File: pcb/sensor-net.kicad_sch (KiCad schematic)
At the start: 14 parts, among them U4 M24C32-FMN, U5 MS5607-02BA, U6 LIS2MDL, U7 LSM6DSO32TR, U8 SAM-M8Q

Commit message: Filled out the BOM for the schematic. Consolidated some components and changed footprint sizes.
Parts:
- C16, C17, C19, C20, C23, C24: footprint Capacitor_SMD:C_0201_0603Metric -> Capacitor_SMD:C_0402_1005Metric; MP (none) -> GRM155R61A104KA01J
- C18: footprint Capacitor_SMD:C_0805_2012Metric -> Capacitor_SMD:C_0603_1608Metric; MP (none) -> C1608X5R0J106K080AB
- C21: MP (none) -> 0603B204K160CT
- C22: MP (none) -> CGA3E1X5R0J475K080AC
- U4: MP (none) -> M24C32-FMN6TP
- U5: MP (none) -> MS560702BA03-50
- U6: MP (none) -> LIS2MDLTR
- U7: MP (none) -> LSM6DSO32TR
- U8: MP (none) -> SAM-M8Q-0
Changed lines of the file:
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@@
 			)
 		)
-		(property "Datasheet" "~"
+		(property "Datasheet" "https://www.mouser.ca/datasheet/2/210/WTC_MLCC_General_Purpose-1534899.pdf"
 			(at 152.4 59.69 0)
 			(effects
@@
 			)
 		)
+		(property "MP" "0603B204K160CT"
+			(at 152.4 59.69 0)
+			(effects
+				(font
+					(size 1.27 1.27)
+				)
+				(hide yes)
+			)
+		)
 		(pin "2"
 		)
@@
 			)
 		)
-		(property "Footprint" "Capacitor_SMD:C_0201_0603Metric"
+		(property "Footprint" "Capacitor_SMD:C_0402_1005Metric"
 			(at 249.8852 107.95 0)
 			(effects
@@
 			)
 		)
-		(property "Datasheet" "~"
+		(property "Datasheet" "https://www.mouser.ca/datasheet/2/281/1/GRM155R61A104KA01_02A-1983866.pdf"
 			(at 248.92 104.14 0)
 			(effects
@@
 			)
 		)
+		(property "MP" "GRM155R61A104KA01J "
+			(at 248.92 104.14 0)
+			(effects
+				(font
+					(size 1.27 1.27)
+				)
+				(hide yes)
+			)
+		)
 		(pin "1"
 		)
@@
 			)
 		)
-		(property "Footprint" "Capacitor_SMD:C_0805_2012Metric"
+		(property "Footprint" "Capacitor_SMD:C_0603_1608Metric"
 			(at 176.2252 43.18 0)
 			(effects
@@
 			)
 		)
-		(property "Datasheet" "~"
+		(property "Datasheet" "https://product.tdk.com/system/files/dam/doc/product/capacitor/ceramic/mlcc/catalog/mlcc_commercial_general_en.pdf?ref_disty=mouser"
 			(at 175.26 39.37 0)
 			(effects
@@
 			)
 		)
+		(property "MP" "C1608X5R0J106K080AB"
+			(at 175.26 39.37 0)
+			(effects
+				(font
+					(size 1.27 1.27)
+				)
+				(hide yes)
+			)
+		)
 		(pin "2"
 		)
@@
 			)
 		)
+		(property "MP" "M24C32-FMN6TP"
+			(at 226.06 48.26 0)
+			(effects
+				(font
+					(size 1.27 1.27)
+				)
+				(hide yes)
+			)
+		)
 		(pin "8"
 		)
@@
 			)
 		)
+		(property "MP" "LIS2MDLTR"
+			(at 137.16 50.8 0)
+			(effects
+				(font
+					(size 1.27 1.27)
+				)
+				(hide yes)
+			)
+		)
 		(pin "9"
 		)
@@
 			)
 		)
-		(property "Footprint" "Capacitor_SMD:C_0201_0603Metric"
+		(property "Footprint" "Capacitor_SMD:C_0402_1005Metric"
 			(at 164.7952 43.18 0)
 			(effects
@@
 			)
 		)
-		(property "Datasheet" "~"
+		(property "Datasheet" "https://www.mouser.ca/datasheet/2/281/1/GRM155R61A104KA01_02A-1983866.pdf"
 			(at 163.83 39.37 0)
 			(effects
@@
 			)
 		)
+		(property "MP" "GRM155R61A104KA01J "
+			(at 163.83 39.37 0)
+			(effects
+				(font
+					(size 1.27 1.27)
+				)
+				(hide yes)
+			)
+		)
 		(pin "2"
 		)
@@
 			)
 		)
-		(property "Footprint" "Capacitor_SMD:C_0201_0603Metric"
+		(property "Footprint" "Capacitor_SMD:C_0402_1005Metric"
 			(at 238.4552 107.95 0)
 			(effects
@@
 			)
 		)
-		(property "Datasheet" "~"
+		(property "Datasheet" "https://www.mouser.ca/datasheet/2/281/1/GRM155R61A104KA01_02A-1983866.pdf"
 			(at 237.49 104.14 0)
 			(effects
@@
 			)
 		)
+		(property "MP" "GRM155R61A104KA01J "
+			(at 237.49 104.14 0)
+			(effects
+				(font
+					(size 1.27 1.27)
+				)
+				(hide yes)
+			)
+		)
 		(pin "1"
 		)
@@
 			)
 		)
-		(property "Footprint" "Capacitor_SMD:C_0201_0603Metric"
+		(property "Footprint" "Capacitor_SMD:C_0402_1005Metric"
 			(at 152.0952 43.18 0)
 			(effects
@@
 			)
 		)
-		(property "Datasheet" "~"
+		(property "Datasheet" "https://www.mouser.ca/datasheet/2/281/1/GRM155R61A104KA01_02A-1983866.pdf"
 			(at 151.13 39.37 0)
 			(effects
@@
 			)
 		)
+		(property "MP" "GRM155R61A104KA01J "
+			(at 151.13 39.37 0)
+			(effects
+				(font
+					(size 1.27 1.27)
+				)
+				(hide yes)
+			)
+		)
 		(pin "2"
 		)
@@
 			)
 		)
-		(property "Footprint" "Capacitor_SMD:C_0201_0603Metric"
+		(property "Footprint" "Capacitor_SMD:C_0402_1005Metric"
 			(at 82.2452 54.61 0)
 			(effects
@@
 			)
 		)
-		(property "Datasheet" "~"
+		(property "Datasheet" "https://www.mouser.ca/datasheet/2/281/1/GRM155R61A104KA01_02A-1983866.pdf"
 			(at 81.28 50.8 0)
 			(effects
@@
 			)
 		)
+		(property "MP" "GRM155R61A104KA01J "
+			(at 81.28 50.8 0)
+			(effects
+				(font
+					(size 1.27 1.27)
+				)
+				(hide yes)
+			)
+		)
 		(pin "2"
 		)
@@
 			)
 		)
-		(property "Datasheet" "~"
+		(property "Datasheet" "https://product.tdk.com/system/files/dam/doc/product/capacitor/ceramic/mlcc/catalog/mlcc_automotive_general_en.pdf?ref_disty=mouser"
 			(at 88.9 96.52 0)
 			(effects
@@
 			)
 		)
+		(property "MP" "CGA3E1X5R0J475K080AC"
+			(at 88.9 96.52 0)
+			(effects
+				(font
+					(size 1.27 1.27)
+				)
+				(hide yes)
+			)
+		)
 		(pin "2"
 		)
@@
 			)
 		)
+		(property "MP" "MS560702BA03-50"
+			(at 63.5 49.53 0)
+			(effects
+				(font
+					(size 1.27 1.27)
+				)
+				(hide yes)
+			)
+		)
 		(pin "8"
 		)
@@
 			)
 		)
-		(property "Footprint" "Capacitor_SMD:C_0201_0603Metric"
+		(property "Footprint" "Capacitor_SMD:C_0402_1005Metric"
 			(at 211.7852 46.99 0)
 			(effects
@@
 			)
 		)
-		(property "Datasheet" "~"
+		(property "Datasheet" "https://www.mouser.ca/datasheet/2/281/1/GRM155R61A104KA01_02A-1983866.pdf"
 			(at 210.82 43.18 0)
 			(effects
@@
 			)
 		)
+		(property "MP" "GRM155R61A104KA01J "
+			(at 210.82 43.18 0)
+			(effects
+				(font
+					(size 1.27 1.27)
+				)
+				(hide yes)
+			)
+		)
 		(pin "1"
 		)
@@
 			)
 		)
+		(property "MP" "SAM-M8Q-0"
+			(at 71.12 114.3 0)
+			(effects
+				(font
+					(size 1.27 1.27)
+				)
+				(hide yes)
+			)
+		)
 		(pin "11"
 		)
@@
 			)
 		)
-		(property "Datasheet" ""
+		(property "Datasheet" "https://www.mouser.ca/datasheet/2/389/lsm6dso32-1815462.pdf"
 			(at 212.09 113.03 0)
 			(effects
@@
 				(hide yes)
 			)
+		)
+		(property "MP" "LSM6DSO32TR"
+			(at 212.09 113.03 0)
+			(effects
+				(font
+					(size 1.27 1.27)
+				)
+				(hide yes)
+			)

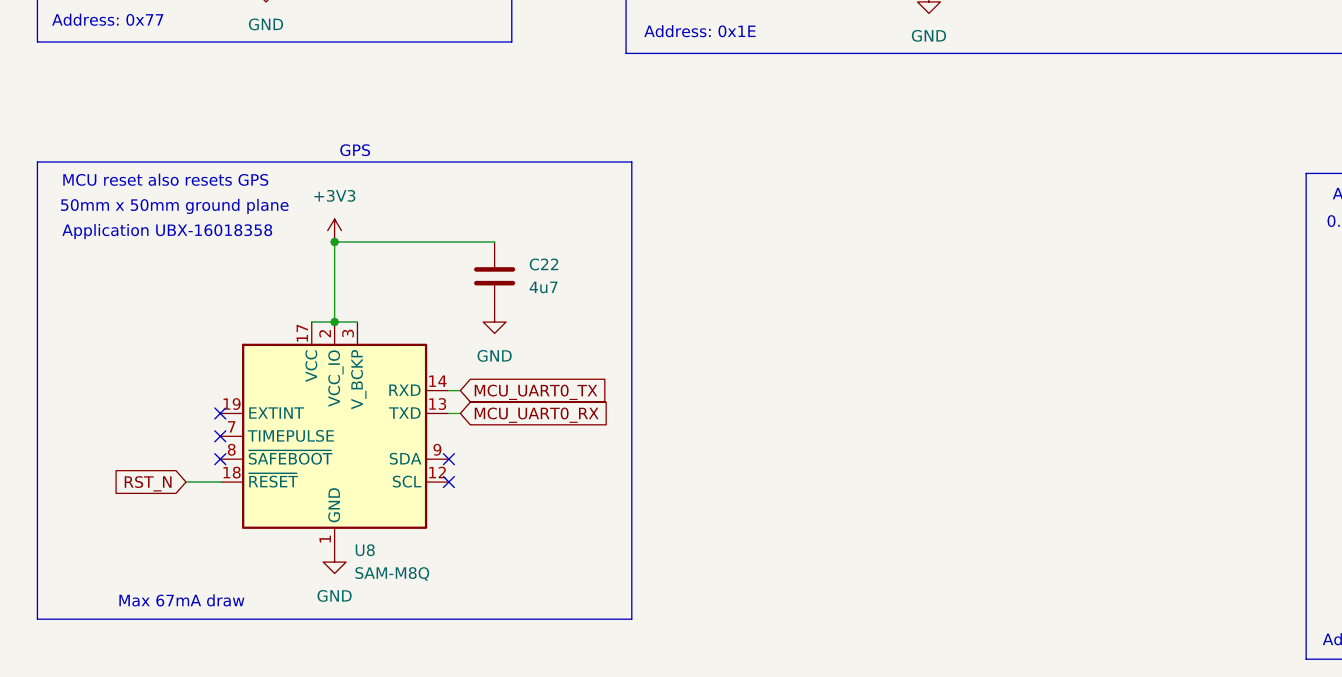
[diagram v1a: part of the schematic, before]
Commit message: Updated GPS to L86G
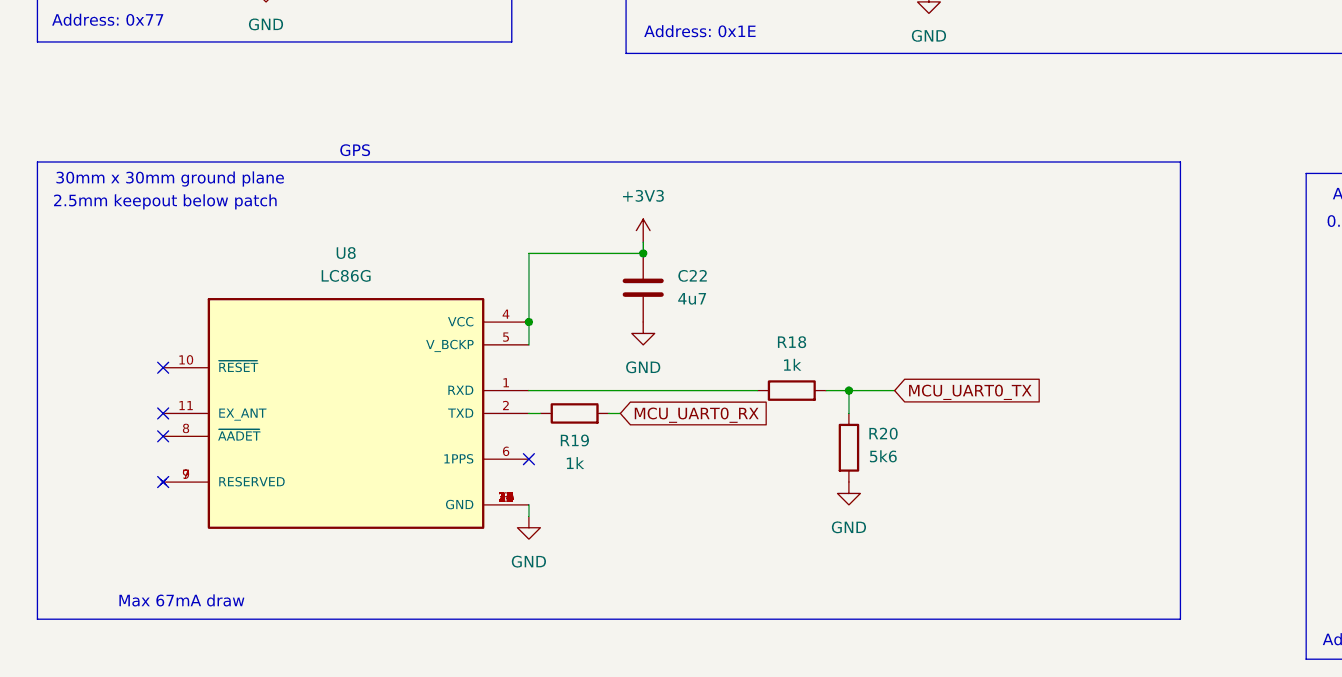
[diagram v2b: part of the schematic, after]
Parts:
- removed U8: SAM-M8Q, RF_GPS:ublox_SAM-M8Q, symbol RF_GPS:SAM-M8Q
- added R18, R19: 1k, Resistor_SMD:R_0402_1005Metric, symbol Device:R
- added R20: 5k6, Resistor_SMD:R_0402_1005Metric, symbol Device:R
- added U8: LC86G, LC86G:XCVR_LC86G, symbol LC86G:LC86G
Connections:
- net +3V3: now also U8.4 (VCC), U8.5 (V_BCKP)
- net GND: now also R20.2, U8.12 (GND), U8.13 (GND), U8.14 (GND), U8.15 (GND), U8.16 (GND), U8.17 (GND), U8.18 (GND), U8.19 (GND), U8.20 (GND), U8.21 (GND), U8.22 (GND), U8.23 (GND), U8.24 (GND), U8.25 (GND), U8.26 (GND), U8.27 (GND), U8.28 (GND), U8.29 (GND), U8.3 (GND), U8.30 (GND), U8.31 (GND), U8.32 (GND), U8.33 (GND), U8.34 (GND), U8.35 (GND), U8.36 (GND)
- net MCU_UART0_RX: now also R19.2
- net MCU_UART0_TX: now also R18.2, R20.1
- new net: R18.1, U8.1 (RXD)
- new net: R19.1, U8.2 (TXD)
- new net: U8.7 (RESERVED), U8.9 (RESERVED)
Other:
- note added: "2.5mm keepout below patch"
- note added: "30mm x 30mm ground plane"
- note removed: "50mm x 50mm ground plane"
- note removed: "Application UBX-16018358"
- note removed: "MCU reset also resets GPS"
- moved on the sheet: C22

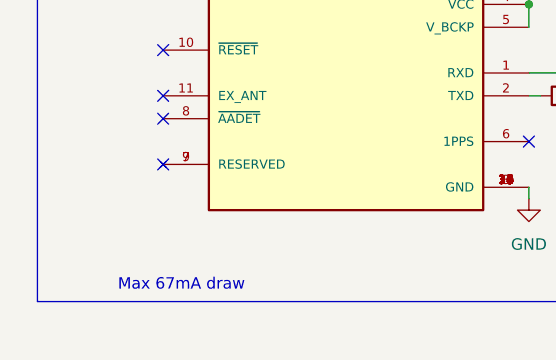
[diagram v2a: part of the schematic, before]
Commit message: Added mounting holes and copper pours.
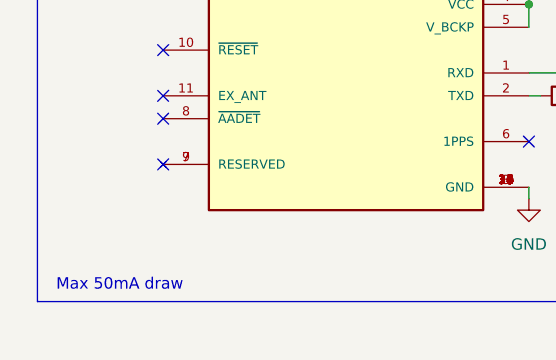
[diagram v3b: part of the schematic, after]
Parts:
- U8: MP LC86G -> LC86GLAMD
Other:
- note added: "Max 50mA draw"
- note removed: "Max 67mA draw"
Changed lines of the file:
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@@
 		)
 	)
-	(text "Max 67mA draw"
-		(exclude_from_sim no)
-		(at 54.102 132.842 0)
+	(text "Max 50mA draw"
+		(exclude_from_sim no)
+		(at 47.244 132.842 0)
 		(effects
 			(font
@@
 			)
 		)
-		(property "Datasheet" ""
+		(property "Datasheet" "https://www.mouser.ca/datasheet/2/1052/Quectel_7_14_2022_Quectel_LC86G_GNSS_Specification-3000079.pdf"
 			(at 72.39 111.76 0)
 			(effects
@@
 			)
 		)
-		(property "MP" "LC86G"
+		(property "MP" "LC86GLAMD"
 			(at 72.39 111.76 0)
 			(effects

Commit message: Added interrupt lines for IMU and magnetometer
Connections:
- net MAG_INT: now reaches U6.7 (DRDY)
- net GYRO_INT: now reaches U7.4 (INT1)
- net XL_INT: now reaches U7.9 (INT2)
- no-connect marks 9 -> 6
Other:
- moved on the sheet: C23, C24, U7

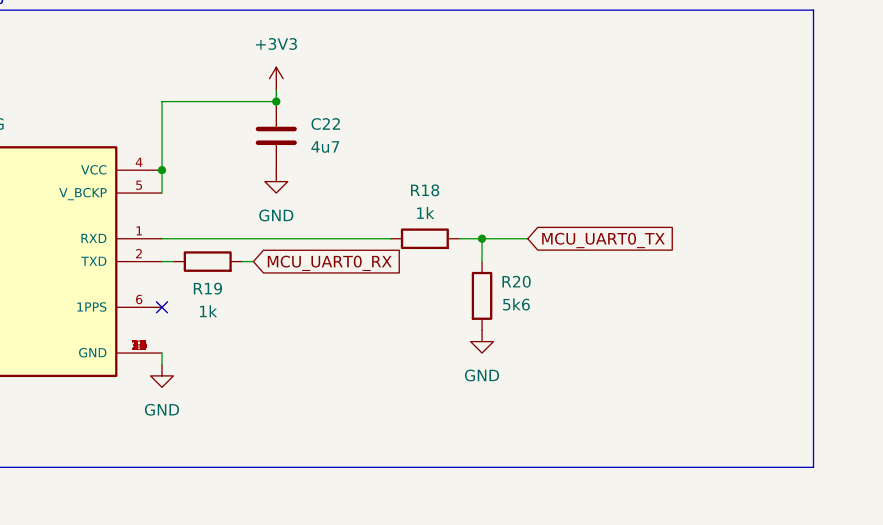
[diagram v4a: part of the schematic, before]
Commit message: Changed LED resistors to 330 ohms to reduce brightness.
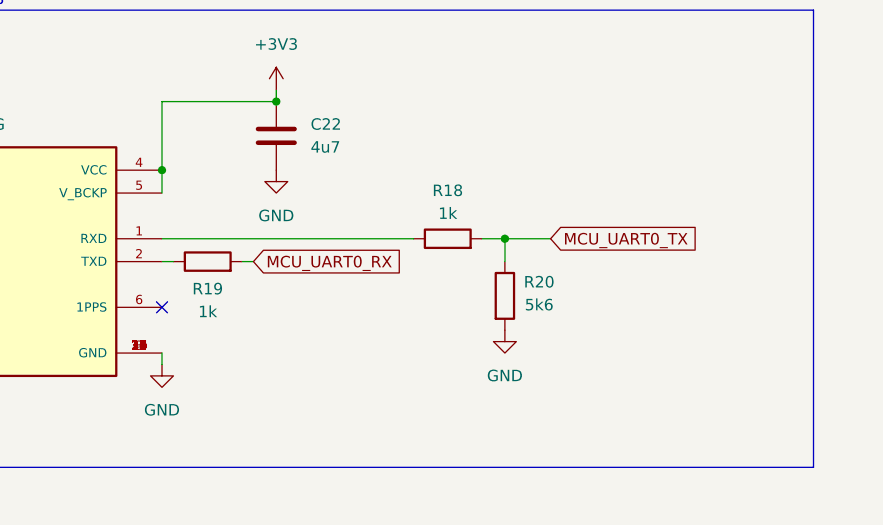
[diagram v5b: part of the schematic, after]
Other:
- moved on the sheet: R18, R20
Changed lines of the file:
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@@
 	)
 	(junction
-		(at 128.27 109.22)
+		(at 130.81 109.22)
 		(diameter 0)
 		(color 0 0 0 0)
@@
 	(wire
 		(pts
-			(xy 128.27 109.22) (xy 133.35 109.22)
+			(xy 130.81 109.22) (xy 135.89 109.22)
 		)
 		(stroke
@@
 	(wire
 		(pts
-			(xy 128.27 111.76) (xy 128.27 109.22)
+			(xy 130.81 111.76) (xy 130.81 109.22)
 		)
 		(stroke
@@
 	(wire
 		(pts
-			(xy 92.71 109.22) (xy 118.11 109.22)
+			(xy 92.71 109.22) (xy 120.65 109.22)
 		)
 		(stroke
@@
 	(wire
 		(pts
-			(xy 128.27 109.22) (xy 125.73 109.22)
+			(xy 130.81 109.22) (xy 128.27 109.22)
 		)
 		(stroke
@@
 	(global_label "MCU_UART0_TX"
 		(shape input)
-		(at 133.35 109.22 0)
+		(at 135.89 109.22 0)
 		(fields_autoplaced yes)
 		(effects
@@
 		)
 		(property "Intersheetrefs" "${INTERSHEET_REFS}"
-			(at 150.3656 109.22 0)
+			(at 152.9056 109.22 0)
 			(effects
 				(font
@@
 	(symbol
 		(lib_id "Device:R")
-		(at 121.92 109.22 90)
+		(at 124.46 109.22 90)
 		(unit 1)
 		(exclude_from_sim no)
@@
 		(dnp no)
 		(property "Reference" "R18"
-			(at 121.92 103.886 90)
+			(at 124.46 103.886 90)
 			(effects
 				(font
@@
 		)
 		(property "Value" "1k"
-			(at 121.92 106.426 90)
+			(at 124.46 106.426 90)
 			(effects
 				(font
@@
 		)
 		(property "Footprint" "Resistor_SMD:R_0402_1005Metric"
-			(at 121.92 110.998 90)
+			(at 124.46 110.998 90)
 			(effects
 				(font
@@
 			)
 		)
-		(property "Datasheet" "~"
-			(at 121.92 109.22 0)
+		(property "Datasheet" "https://www.mouser.ca/datasheet/2/315/AOA0000C307-1149632.pdf"
+			(at 124.46 109.22 0)
 			(effects
 				(font
@@
 		)
 		(property "Description" "Resistor"
-			(at 121.92 109.22 0)
+			(at 124.46 109.22 0)
 			(effects
 				(font
@@
 		)
 		(property "MP" "ERA-2AEB102X"
-			(at 121.92 109.22 0)
+			(at 124.46 109.22 0)
 			(effects
 				(font
@@
 			)
 		)
-		(property "Datasheet" "~"
+		(property "Datasheet" "https://www.mouser.ca/datasheet/2/315/AOA0000C307-1149632.pdf"
 			(at 97.79 111.76 0)
 			(effects
@@
 	(symbol
 		(lib_id "Device:R")
-		(at 128.27 115.57 0)
+		(at 130.81 115.57 0)
 		(unit 1)
 		(exclude_from_sim no)
@@
 		(dnp no)
 		(property "Reference" "R20"
-			(at 132.08 114.046 0)
+			(at 134.62 114.046 0)
 			(effects
 				(font
@@
 		)
 		(property "Value" "5k6"
-			(at 132.08 116.586 0)
+			(at 134.62 116.586 0)
 			(effects
 				(font
@@
 		)
 		(property "Footprint" "Resistor_SMD:R_0402_1005Metric"
-			(at 126.492 115.57 90)
+			(at 129.032 115.57 90)
 			(effects
 				(font
@@
 		)
 		(property "Datasheet" "https://www.mouser.ca/datasheet/2/54/cr-1858361.pdf"
-			(at 128.27 115.57 0)
+			(at 130.81 115.57 0)
 			(effects
 				(font
@@
 		)
 		(property "Description" "Resistor"
-			(at 128.27 115.57 0)
+			(at 130.81 115.57 0)
 			(effects
 				(font
@@
 		)
 		(property "MP" "CR0402-FX-5601GLF"
-			(at 128.27 115.57 0)
+			(at 130.81 115.57 0)
 			(effects
 				(font
@@
 	(symbol
 		(lib_id "power:GND")
-		(at 128.27 119.38 0)
+		(at 130.81 119.38 0)
 		(unit 1)
 		(exclude_from_sim no)
@@
 		(fields_autoplaced yes)
 		(property "Reference" "#PWR075"
-			(at 128.27 125.73 0)
+			(at 130.81 125.73 0)
 			(effects
 				(font
@@
 		)
 		(property "Value" "GND"
-			(at 128.27 124.46 0)
+			(at 130.81 124.46 0)
 			(effects
 				(font
@@
 		)
 		(property "Footprint" ""
-			(at 128.27 119.38 0)
+			(at 130.81 119.38 0)
 			(effects
 				(font
@@
 		)
 		(property "Datasheet" ""
-			(at 128.27 119.38 0)
+			(at 130.81 119.38 0)
 			(effects
 				(font
@@
 		)
 		(property "Description" "Power symbol creates a global label with name \"GND\" , ground"
-			(at 128.27 119.38 0)
+			(at 130.81 119.38 0)
 			(effects
 				(font
